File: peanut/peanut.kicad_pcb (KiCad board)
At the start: 4 copper layers, 48.2 x 24.5 mm, 74 parts, among them J1 USB-C, J2 PYRO_OUT, J3 Battery JST, J4 Arming, Q1 NMOS, Q2 NMOS, Q3 NMOS, Q4 NMOS, Q5 PMOS, U1 MS5611-01BA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

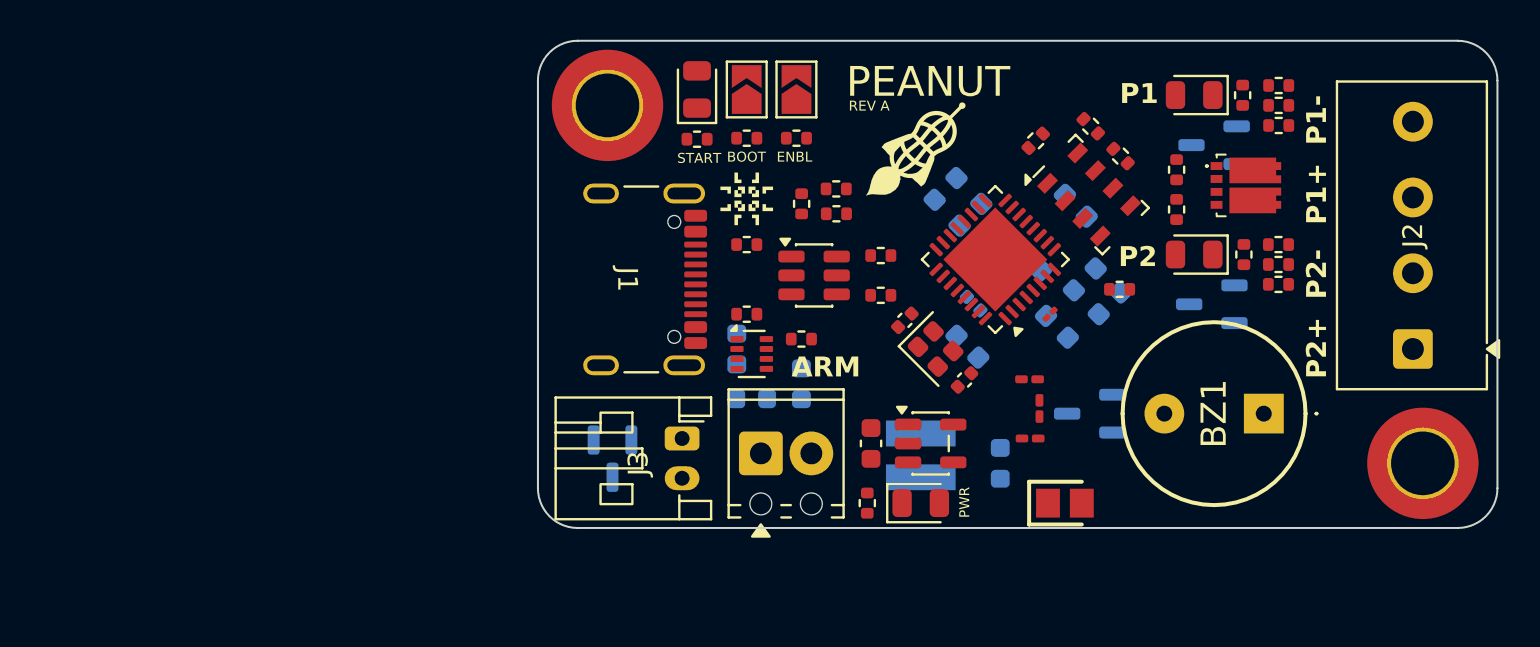
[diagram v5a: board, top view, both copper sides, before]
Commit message: feat: Initial routing
Initial, rough routing of traces.
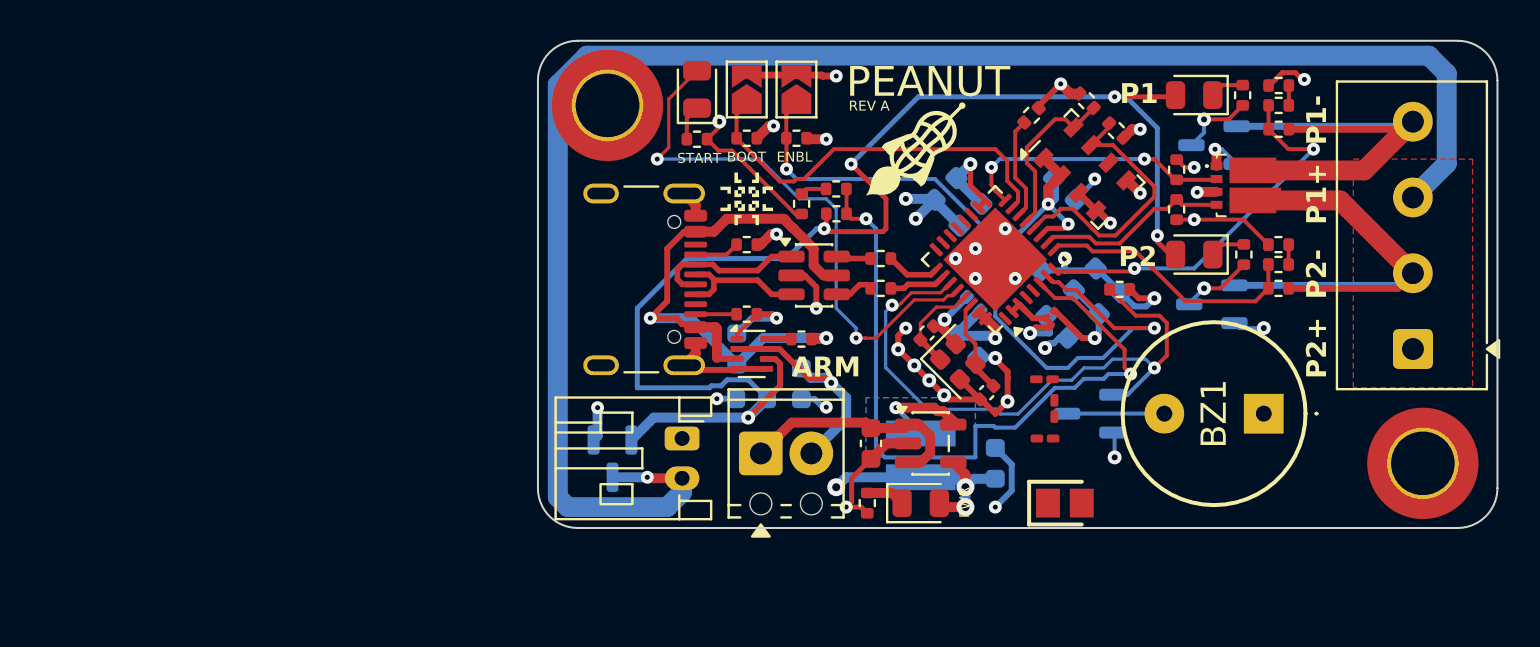
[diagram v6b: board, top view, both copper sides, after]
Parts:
- moved R25 1.30 mm to (149.1, 89.5)
- moved R26 1.30 mm to (147.6, 88.0)
- moved R8 1.30 mm to (144.8, 88.7)
- moved U1 1.30 mm to (147.5, 91.4)
- moved C1 1.29 mm to (139.6, 99.7)
- moved Y1 1.29 mm to (141.1, 101.1)
- moved C2 1.29 mm to (142.6, 102.7)
- moved C3 1.01 mm to (146.5, 92.4)
- moved C12 0.75 mm to (145.5, 102.0)
- moved C13 0.75 mm to (145.5, 105.0)
- moved L2 0.75 mm to (146.0, 103.5)
- moved R6 0.35 mm to (137.2, 97.4)
- moved C15 0.25 mm to (143.0, 106.2)
- moved R14 0.20 mm to (157.2, 97.4), turned to 180 degrees
- moved R10 0.19 mm to (157.2, 89.4)
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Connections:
- net Net-(R5-Pad1) renamed /PROT_D-
- net Net-(R6-Pad1) renamed /PROT_D+
- Q4 pad 10: (no net) -> /Pyro Channels/PYRO_1-
- Q4 pad 9: (no net) -> /Pyro Channels/PYRO_2-
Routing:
- net GND: track 0.00 -> 92.4 mm, vias 0 -> 38
- net VBAT_RAW: track 0.00 -> 84.3 mm, vias 0 -> 1
- net VBAT: track 0.00 -> 69.4 mm, vias 0 -> 5
- net 3V3: track 0.00 -> 45.2 mm, vias 0 -> 12
- net BAT_MON: track 0.00 -> 36.8 mm, vias 0 -> 2
- net /ENABLE: track 0.00 -> 35.7 mm, vias 0 -> 2
- net VUSB: track 0.00 -> 31.8 mm, vias 0 -> 2
- net /BUZ_PWM: track 0.00 -> 31.5 mm, vias 0 -> 2
- net /START: track 0.00 -> 28.3 mm, vias 0 -> 2
- net /Pyro Channels/PYRO_2-: track 0.00 -> 26.0 mm
- net /Pyro Channels/PYRO_1-: track 0.00 -> 25.1 mm
- net /BOOT: track 0.00 -> 20.0 mm
- net PYRO_1_CONT: track 0.00 -> 19.5 mm, vias 0 -> 2
- net PYRO_1_TRIGGER: track 0.00 -> 14.1 mm, vias 0 -> 2
- net /I2C_SDA: track 0.00 -> 13.7 mm
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- added copper zone on B.Cu, net Net-(U4-SW)
- added copper zone on F.Cu, net VBAT_RAW

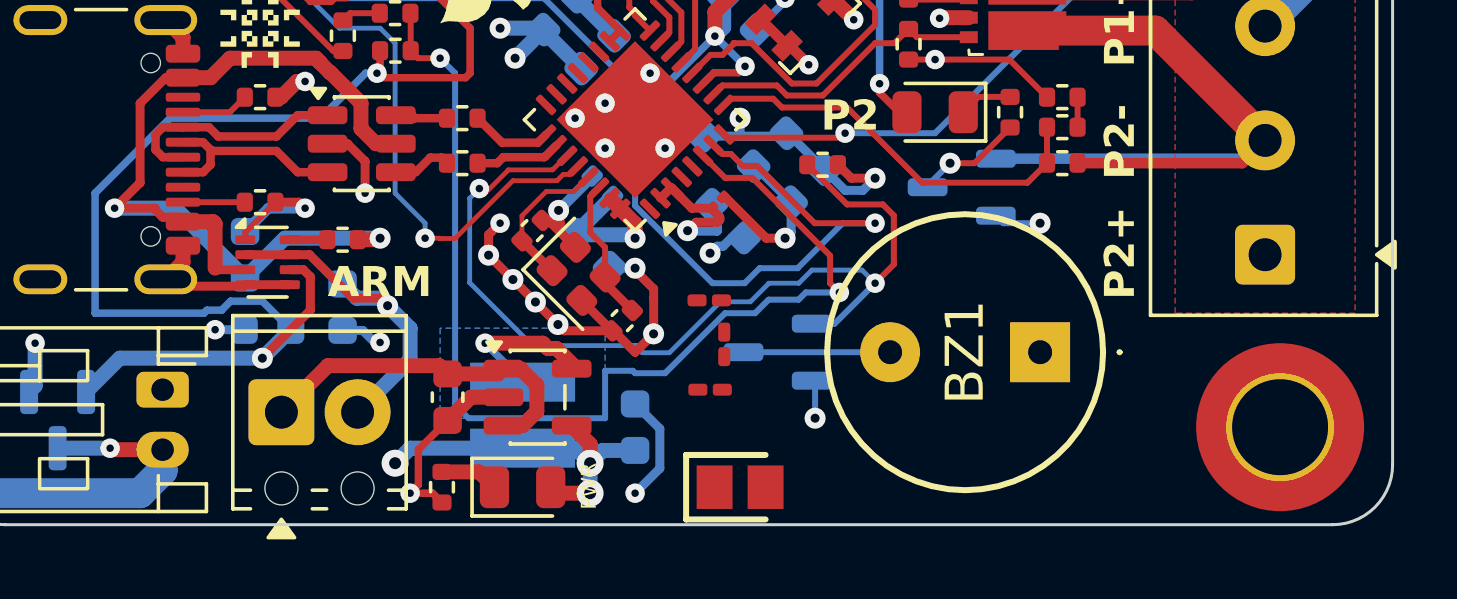
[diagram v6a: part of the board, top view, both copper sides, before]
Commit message: chore: Fix all DRC issues except RF routing
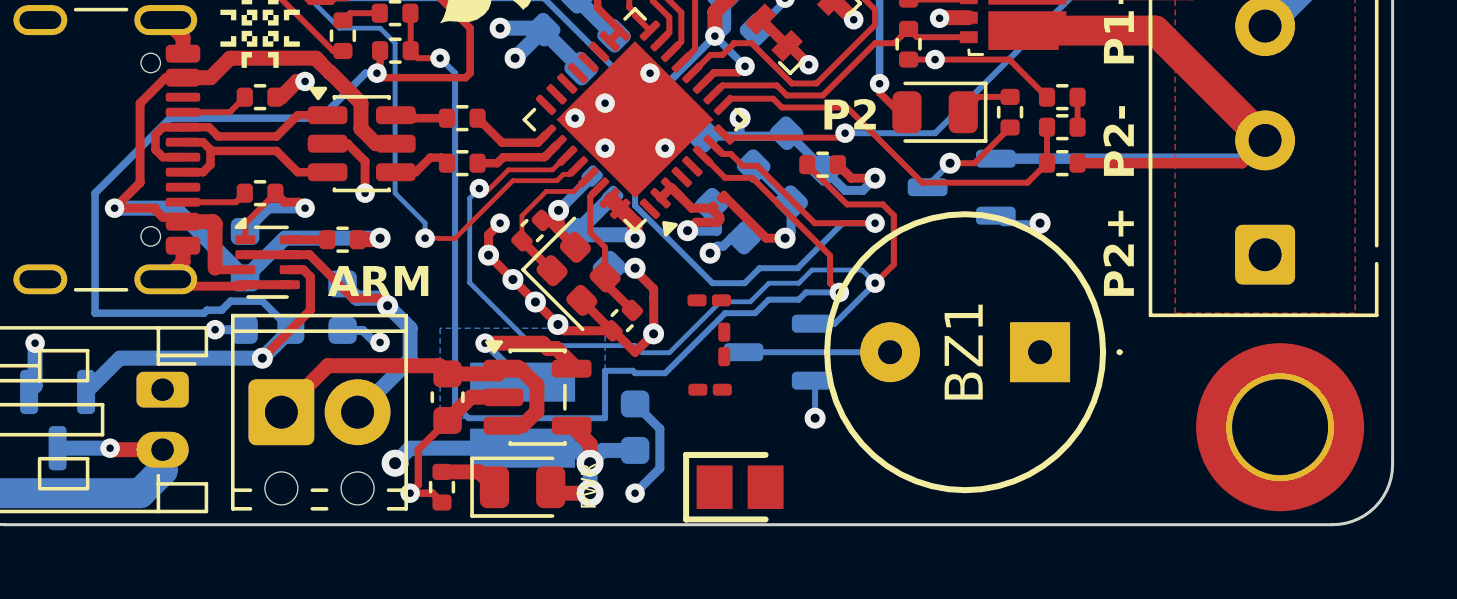
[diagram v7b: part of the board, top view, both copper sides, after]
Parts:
- moved R4 0.30 mm to (130.5, 98.4)

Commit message: feat: Open Source Hardware silkscreen
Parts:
- added REF**: OSHW-Logo_5.7x6mm_SilkScreen, Symbol:OSHW-Logo_5.7x6mm_SilkScreen, B.Cu at (125.9, 97.0)
